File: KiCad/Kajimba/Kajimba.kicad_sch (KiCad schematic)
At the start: 19 parts, among them J1 Barrel Jack, J2 Pump, J3 Sensor, J4 Screen, J5 Button, Q1 QM6006D, SW1 Button, U1 Pico, U2 LM78M05

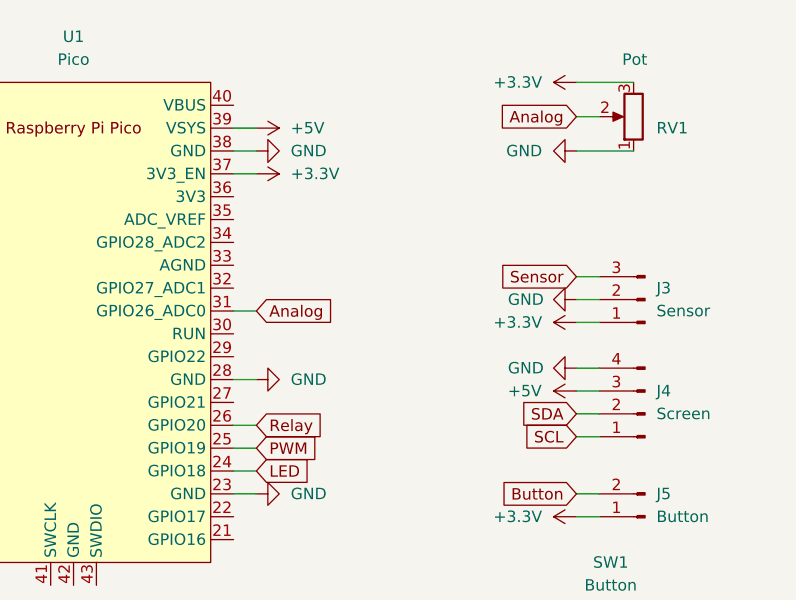
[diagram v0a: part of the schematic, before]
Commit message: v05
moved pin 3.3v_en to 3.3v
switched pins on 3 pin jst connector
cleaned up circuit diagram sheet
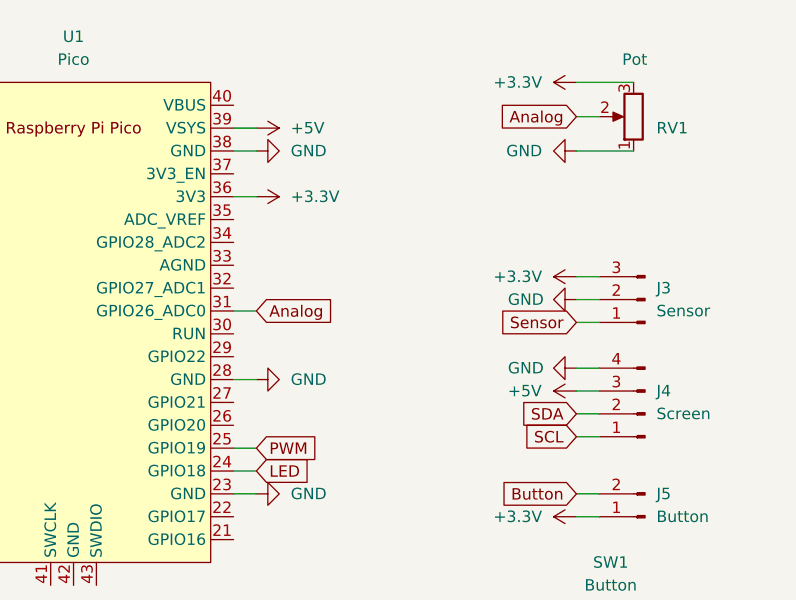
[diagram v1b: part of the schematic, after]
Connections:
- net +3.3V: now also J3.3 (Pin_3), U1.36 (3V3); no longer J3.1 (Pin_1), U1.37 (3V3_EN)
- net Sensor: now also J3.1 (Pin_1); no longer J3.3 (Pin_3)
- net Relay: no longer names the net of U1.26 (GPIO20)

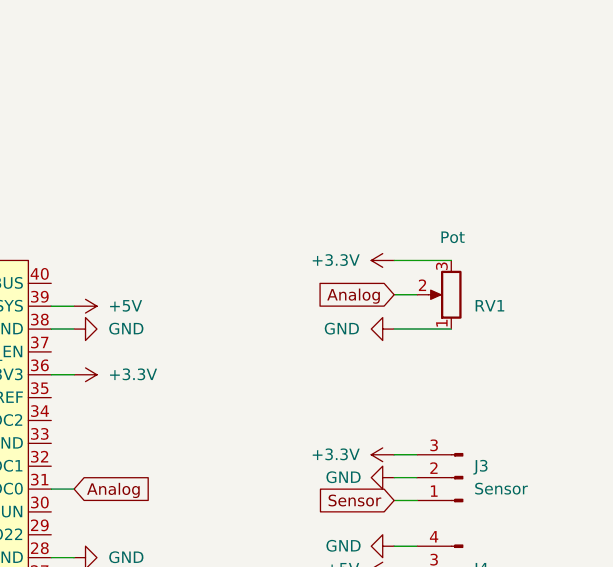
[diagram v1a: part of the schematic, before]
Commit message: v06 KiCad
removed pot
moved button / IO around
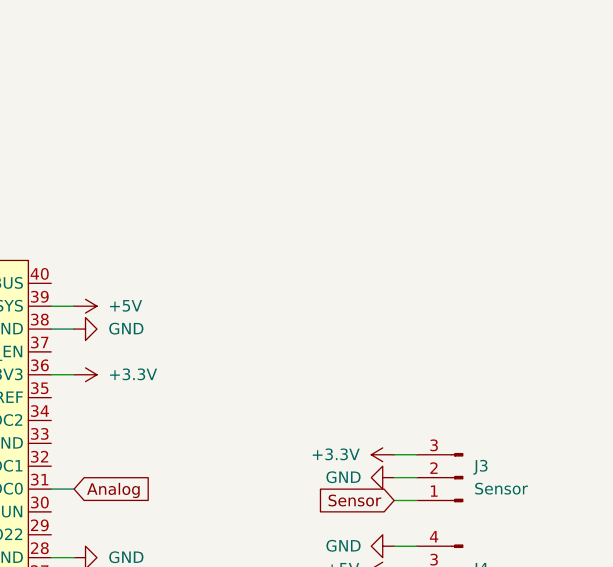
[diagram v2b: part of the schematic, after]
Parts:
- removed RV1: Pot, Potentiometer_THT:Potentiometer_Bourns_3296W_Vertical, symbol Device:R_Potentiometer
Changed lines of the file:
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@@
   (title_block
     (title "Pump")
-    (date "2022-12-22")
-    (rev "v05")
+    (date "2023-01-18")
+    (rev "v06")
     (company "Kajimba")
     (comment 1 "Author: Yael")
@@
     (stroke (width 0) (type default) (color 0 0 0 0))
   )
-  (wire (pts (xy 237.49 74.93) (xy 231.14 74.93))
-    (stroke (width 0) (type default) (color 0 0 0 0))
-  )
   (wire (pts (xy 99.06 68.58) (xy 113.03 68.58))
     (stroke (width 0) (type default) (color 0 0 0 0))
   )
-  (wire (pts (xy 233.68 78.74) (xy 231.14 78.74))
-    (stroke (width 0) (type default) (color 0 0 0 0))
-  )
   (wire (pts (xy 85.09 49.53) (xy 85.09 55.88))
     (stroke (width 0) (type default) (color 0 0 0 0))
@@
   )
   (wire (pts (xy 231.14 101.6) (xy 233.68 101.6))
-    (stroke (width 0) (type default) (color 0 0 0 0))
-  )
-  (wire (pts (xy 237.49 82.55) (xy 231.14 82.55))
     (stroke (width 0) (type default) (color 0 0 0 0))
   )
@@
     )
   )
-  (global_label "Analog" (shape input) (at 231.14 78.74 180) (fields_autoplaced)
-    (effects (font (size 1.27 1.27)) (justify right))
-    (property "Intersheet References" "${INTERSHEET_REFS}" (id 0) (at 222.3769 78.8194 0)
-      (effects (font (size 1.27 1.27)) (justify right) hide)
-    )
-  )
   (global_label "Sensor" (shape input) (at 231.14 101.6 180) (fields_autoplaced)
     (effects (font (size 1.27 1.27)) (justify right))
@@
     (pin "3")
     (pin "4")
-  )
-  (symbol (lib_id "power:GND") (at 231.14 82.55 270) (unit 1)
-    (in_bom yes) (on_board yes) (fields_autoplaced)
-    (property "Reference" "#PWR018" (id 0) (at 224.79 82.55 0)
-      (effects (font (size 1.27 1.27)) hide)
-    )
-    (property "Value" "GND" (id 1) (at 227.33 82.5501 90)
-      (effects (font (size 1.27 1.27)) (justify right))
-    )
-    (property "Footprint" "" (id 2) (at 231.14 82.55 0)
-      (effects (font (size 1.27 1.27)) hide)
-    )
-    (property "Datasheet" "" (id 3) (at 231.14 82.55 0)
-      (effects (font (size 1.27 1.27)) hide)
-    )
-    (pin "1")
   )
   (symbol (lib_id "power:GND") (at 123.19 71.12 0) (unit 1)
@@
     (pin "1")
   )
-  (symbol (lib_id "Device:R_Potentiometer") (at 237.49 78.74 180) (unit 1)
-    (in_bom yes) (on_board yes)
-    (property "Reference" "RV1" (id 0) (at 240.03 80.0101 0)
-      (effects (font (size 1.27 1.27)) (justify right))
-    )
-    (property "Value" "Pot" (id 1) (at 236.22 72.39 0)
-      (effects (font (size 1.27 1.27)) (justify right))
-    )
-    (property "Footprint" "Potentiometer_THT:Potentiometer_Bourns_3296W_Vertical" (id 2) (at 237.49 78.74 0)
-      (effects (font (size 1.27 1.27)) hide)
-    )
-    (property "Datasheet" "~" (id 3) (at 237.49 78.74 0)
-      (effects (font (size 1.27 1.27)) hide)
-    )
-    (pin "1")
-    (pin "2")
-    (pin "3")
-  )
   (symbol (lib_id "Diode:S2JTR") (at 74.93 49.53 180) (unit 1)
     (in_bom yes) (on_board yes) (fields_autoplaced)
@@
     (pin "1")
   )
-  (symbol (lib_id "power:+3.3V") (at 231.14 74.93 90) (unit 1)
-    (in_bom yes) (on_board yes)
-    (property "Reference" "#PWR0101" (id 0) (at 234.95 74.93 0)
-      (effects (font (size 1.27 1.27)) hide)
-    )
-    (property "Value" "+3.3V" (id 1) (at 227.33 74.9301 90)
-      (effects (font (size 1.27 1.27)) (justify left))
-    )
-    (property "Footprint" "" (id 2) (at 231.14 74.93 0)
-      (effects (font (size 1.27 1.27)) hide)
-    )
-    (property "Datasheet" "" (id 3) (at 231.14 74.93 0)
-      (effects (font (size 1.27 1.27)) hide)
-    )
-    (pin "1")
-  )
   (symbol (lib_id "power:+3.3V") (at 231.14 123.19 90) (unit 1)
     (in_bom yes) (on_board yes)
@@
       (reference "#PWR016") (unit 1) (value "GND") (footprint "")
     )
-    (path "/5cca70b3-4b83-4ba5-96bc-80be6ca77d83"
-      (reference "#PWR018") (unit 1) (value "GND") (footprint "")
-    )
     (path "/30922fc7-89e1-4917-9d99-0d990ce82a44"
       (reference "#PWR019") (unit 1) (value "GND") (footprint "")
@@
       (reference "#PWR025") (unit 1) (value "GND") (footprint "")
     )
-    (path "/9f04ceed-157d-4a97-9d80-da6712d15a44"
-      (reference "#PWR0101") (unit 1) (value "+3.3V") (footprint "")
-    )
     (path "/ff8bf298-1064-4f18-bae7-edf8da7c14bd"
       (reference "C1") (unit 1) (value "470uF") (footprint "Capacitor_SMD:CP_Elec_10x10.5")
@@
       (reference "R3") (unit 1) (value "1.5k") (footprint "Resistor_SMD:R_0805_2012Metric_Pad1.20x1.40mm_HandSolder")
     )
-    (path "/799aa9cc-ff16-444b-892a-5596fefd3c62"
-      (reference "RV1") (unit 1) (value "Pot") (footprint "Potentiometer_THT:Potentiometer_Bourns_3296W_Vertical")
-    )
     (path "/bf7b1cea-090e-421d-a04a-7e7eacdd917e"
